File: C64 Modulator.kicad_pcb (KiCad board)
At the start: 2 copper layers, 63.5 x 63.4 mm, 36 parts, among them J1 Power, J10 , J11 , J12 , J13 , J14 , J2 8765, J3 4321, J4 AUD_STEREO, J5 TRS_3.5mm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

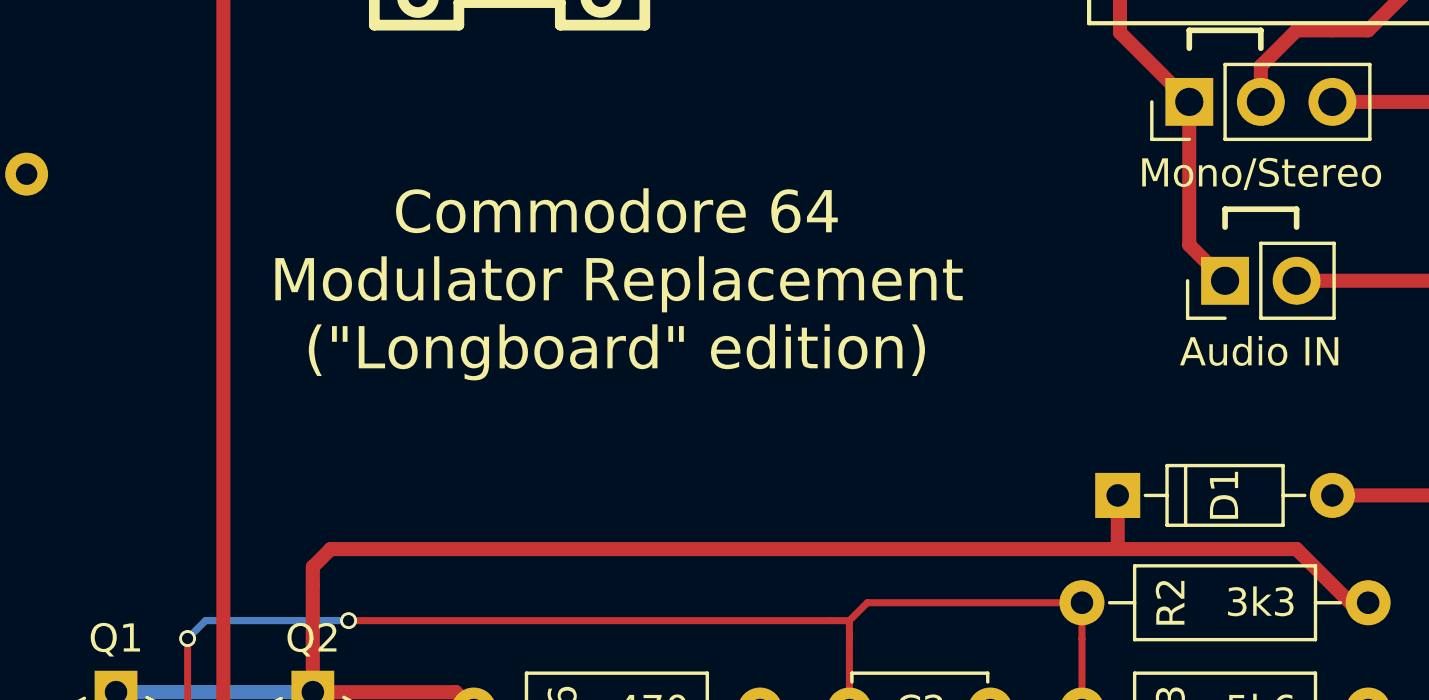
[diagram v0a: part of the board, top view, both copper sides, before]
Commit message: Added component notices to PCB
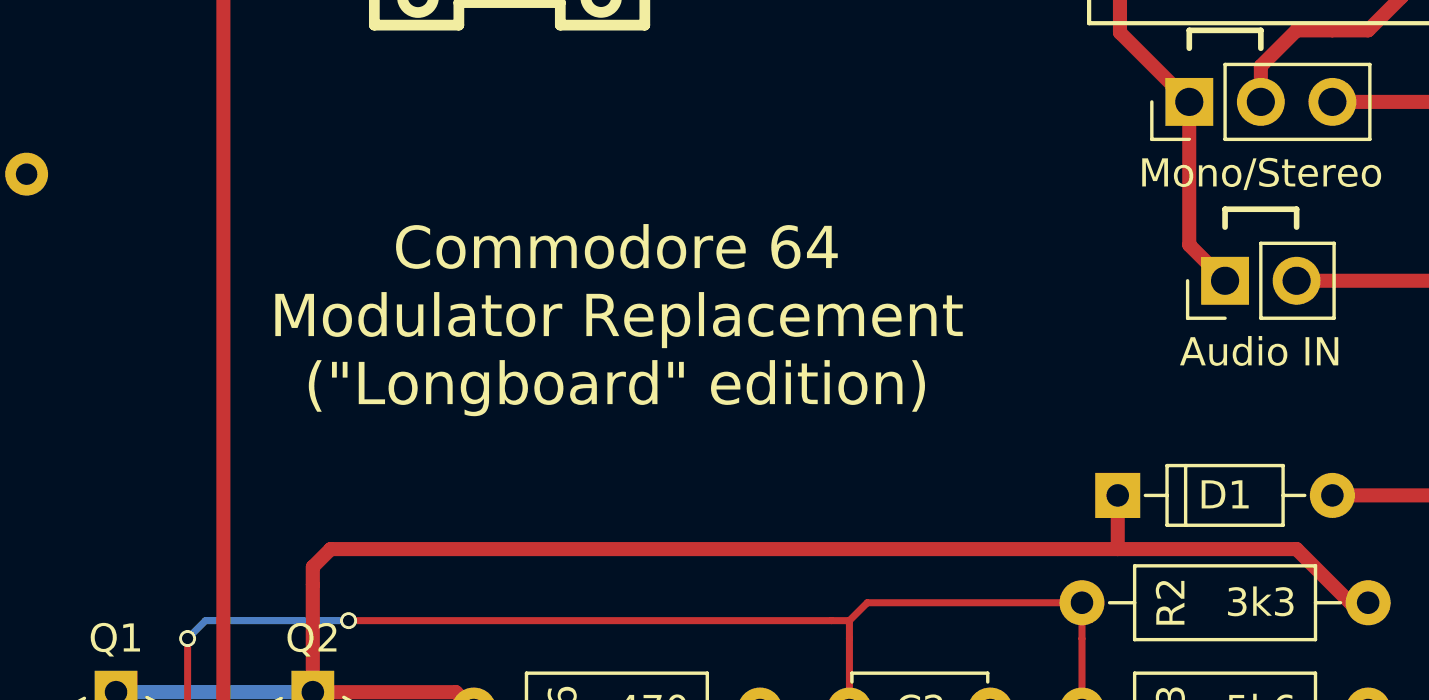
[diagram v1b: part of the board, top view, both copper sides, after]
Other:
- board text added: "L1 & D1 pads can be shorted, C2 & C3 can be left out."
- board text added: "L2, C6, R8, R11 & RCA can be left out if composite video is not required."
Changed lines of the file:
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@@
     (links 53)
     (no_connects 0)
-    (area 113.03 50.092 185.683334 130.175001)
+    (area 118.669999 62.154999 182.360001 125.745001)
     (thickness 1.6)
-    (drawings 54)
+    (drawings 125)
     (tracks 114)
     (zones 0)
@@
       (effects (font (size 1 1) (thickness 0.15)))
     )
-    (fp_text value 68pF (at 2.54 -1.27 180) (layer B.SilkS)
+    (fp_text value 68pF (at 2.54 -1.905 180) (layer B.SilkS)
       (effects (font (size 1 1) (thickness 0.15)) (justify mirror))
     )
@@
     (descr "D, DO-35_SOD27 series, Axial, Horizontal, pin pitch=7.62mm, , length*diameter=4*2mm^2, , http://www.diodes.com/_files/packages/DO-35.pdf")
     (tags "D DO-35_SOD27 series Axial Horizontal pin pitch 7.62mm  length 4mm diameter 2mm")
-    (fp_text reference D1 (at 3.81 0 90) (layer F.SilkS)
-      (effects (font (size 1 1) (thickness 0.15)))
-    )
-    (fp_text value 1n4148 (at 3.81 0) (layer B.SilkS)
+    (fp_text reference D1 (at 3.81 0) (layer F.SilkS)
+      (effects (font (size 1 1) (thickness 0.15)))
+    )
+    (fp_text value 1n4148 (at 3.81 1.27) (layer B.SilkS)
       (effects (font (size 1 1) (thickness 0.15)) (justify mirror))
     )
-    (fp_text user %R (at 3.81 0 90) (layer F.Fab)
+    (fp_text user %R (at 3.81 0 180) (layer F.Fab)
       (effects (font (size 1 1) (thickness 0.15)))
     )
@@
       (effects (font (size 1 1) (thickness 0.15)))
     )
-    (fp_text value 1n4148 (at 3.81 0 180) (layer B.SilkS)
+    (fp_text value 1n4148 (at 3.81 -1.27 180) (layer B.SilkS)
       (effects (font (size 1 1) (thickness 0.15)) (justify mirror))
     )
@@
     )
   )
+  (gr_line (start 165.735 102.235) (end 165.1 102.235) (angle 90) (layer B.SilkS) (width 0.2))
+  (gr_line (start 165.1 101.6) (end 165.735 101.6) (angle 90) (layer B.SilkS) (width 0.2))
+  (gr_line (start 161.925 102.235) (end 161.29 102.235) (angle 90) (layer B.SilkS) (width 0.2))
+  (gr_line (start 161.29 101.6) (end 161.925 101.6) (angle 90) (layer B.SilkS) (width 0.2))
+  (gr_line (start 163.83 102.235) (end 164.465 102.235) (angle 90) (layer B.SilkS) (width 0.2))
+  (gr_line (start 163.83 101.6) (end 164.465 101.6) (angle 90) (layer B.SilkS) (width 0.2))
+  (gr_line (start 164.465 90.17) (end 165.1 90.17) (angle 90) (layer B.SilkS) (width 0.2))
+  (gr_line (start 163.195 90.17) (end 163.83 90.17) (angle 90) (layer B.SilkS) (width 0.2))
+  (gr_line (start 161.925 90.17) (end 162.56 90.17) (angle 90) (layer B.SilkS) (width 0.2))
+  (gr_line (start 162.56 101.6) (end 163.195 101.6) (angle 90) (layer B.SilkS) (width 0.2))
+  (gr_line (start 153.67 86.995) (end 153.67 87.63) (angle 90) (layer B.SilkS) (width 0.2))
+  (gr_line (start 153.67 85.725) (end 153.67 86.36) (angle 90) (layer B.SilkS) (width 0.2))
+  (gr_line (start 153.035 86.995) (end 153.035 87.63) (angle 90) (layer B.SilkS) (width 0.2))
+  (gr_line (start 153.035 85.725) (end 153.035 86.36) (angle 90) (layer B.SilkS) (width 0.2))
+  (gr_line (start 164.465 90.805) (end 165.1 90.805) (angle 90) (layer B.SilkS) (width 0.2))
+  (gr_line (start 163.195 90.805) (end 163.83 90.805) (angle 90) (layer B.SilkS) (width 0.2))
+  (gr_line (start 161.925 90.805) (end 162.56 90.805) (angle 90) (layer B.SilkS) (width 0.2))
+  (gr_line (start 160.655 90.17) (end 161.29 90.805) (angle 90) (layer B.SilkS) (width 0.2))
+  (gr_line (start 160.655 90.805) (end 161.29 90.17) (angle 90) (layer B.SilkS) (width 0.2))
+  (gr_line (start 159.385 101.6) (end 160.02 102.235) (angle 90) (layer B.SilkS) (width 0.2))
+  (gr_line (start 159.385 102.235) (end 160.02 101.6) (angle 90) (layer B.SilkS) (width 0.2))
+  (gr_line (start 153.67 83.185) (end 153.035 83.82) (angle 90) (layer B.SilkS) (width 0.2))
+  (gr_line (start 153.035 83.185) (end 153.67 83.82) (angle 90) (layer B.SilkS) (width 0.2))
+  (gr_line (start 153.035 76.835) (end 153.67 77.47) (angle 90) (layer B.SilkS) (width 0.2))
+  (gr_line (start 153.67 76.835) (end 153.035 76.835) (angle 90) (layer B.SilkS) (width 0.2))
+  (gr_line (start 153.035 77.47) (end 153.67 76.835) (angle 90) (layer B.SilkS) (width 0.2))
+  (gr_line (start 153.67 76.835) (end 153.035 76.835) (angle 90) (layer B.SilkS) (width 0.2))
+  (gr_line (start 153.67 77.47) (end 153.67 76.835) (angle 90) (layer B.SilkS) (width 0.2))
+  (gr_line (start 153.035 77.47) (end 153.67 77.47) (angle 90) (layer B.SilkS) (width 0.2))
+  (gr_line (start 153.035 76.835) (end 153.035 77.47) (angle 90) (layer B.SilkS) (width 0.2))
+  (gr_line (start 137.795 101.6) (end 138.43 102.235) (angle 90) (layer B.SilkS) (width 0.2))
+  (gr_line (start 138.43 101.6) (end 137.795 102.235) (angle 90) (layer B.SilkS) (width 0.2))
+  (gr_line (start 137.795 105.41) (end 138.43 106.045) (angle 90) (layer B.SilkS) (width 0.2))
+  (gr_line (start 137.795 106.045) (end 138.43 105.41) (angle 90) (layer B.SilkS) (width 0.2))
+  (gr_line (start 129.54 109.22) (end 130.175 109.855) (angle 90) (layer B.SilkS) (width 0.2))
+  (gr_line (start 129.54 109.855) (end 130.175 109.22) (angle 90) (layer B.SilkS) (width 0.2))
+  (gr_line (start 137.795 109.22) (end 138.43 109.855) (angle 90) (layer B.SilkS) (width 0.2))
+  (gr_line (start 137.795 109.855) (end 138.43 109.22) (angle 90) (layer B.SilkS) (width 0.2))
+  (gr_line (start 138.43 109.855) (end 137.795 109.855) (angle 90) (layer B.SilkS) (width 0.2))
+  (gr_line (start 138.43 109.22) (end 138.43 109.855) (angle 90) (layer B.SilkS) (width 0.2))
+  (gr_line (start 137.795 109.22) (end 138.43 109.22) (angle 90) (layer B.SilkS) (width 0.2))
+  (gr_line (start 137.795 109.855) (end 137.795 109.22) (angle 90) (layer B.SilkS) (width 0.2))
+  (gr_line (start 138.43 106.045) (end 137.795 106.045) (angle 90) (layer B.SilkS) (width 0.2))
+  (gr_line (start 138.43 105.41) (end 138.43 106.045) (angle 90) (layer B.SilkS) (width 0.2))
+  (gr_line (start 137.795 105.41) (end 138.43 105.41) (angle 90) (layer B.SilkS) (width 0.2))
+  (gr_line (start 137.795 106.045) (end 137.795 105.41) (angle 90) (layer B.SilkS) (width 0.2))
+  (gr_line (start 130.175 109.855) (end 129.54 109.855) (angle 90) (layer B.SilkS) (width 0.2))
+  (gr_line (start 130.175 109.22) (end 130.175 109.855) (angle 90) (layer B.SilkS) (width 0.2))
+  (gr_line (start 129.54 109.22) (end 130.175 109.22) (angle 90) (layer B.SilkS) (width 0.2))
+  (gr_line (start 129.54 109.855) (end 129.54 109.22) (angle 90) (layer B.SilkS) (width 0.2))
+  (gr_line (start 138.43 102.235) (end 137.795 102.235) (angle 90) (layer B.SilkS) (width 0.2))
+  (gr_line (start 138.43 101.6) (end 138.43 102.235) (angle 90) (layer B.SilkS) (width 0.2))
+  (gr_line (start 137.795 101.6) (end 138.43 101.6) (angle 90) (layer B.SilkS) (width 0.2))
+  (gr_line (start 137.795 102.235) (end 137.795 101.6) (angle 90) (layer B.SilkS) (width 0.2))
+  (gr_line (start 150.495 105.41) (end 151.13 106.045) (angle 90) (layer B.SilkS) (width 0.2))
+  (gr_line (start 151.13 105.41) (end 150.495 106.045) (angle 90) (layer B.SilkS) (width 0.2))
+  (gr_line (start 151.13 97.79) (end 150.495 98.425) (angle 90) (layer B.SilkS) (width 0.2))
+  (gr_line (start 150.495 97.79) (end 151.13 98.425) (angle 90) (layer B.SilkS) (width 0.2))
+  (gr_line (start 163.195 102.235) (end 162.56 102.235) (angle 90) (layer B.SilkS) (width 0.2))
+  (gr_line (start 121.92 88.265) (end 121.92 83.185) (angle 90) (layer B.SilkS) (width 0.2))
+  (gr_line (start 152.4 88.265) (end 121.92 88.265) (angle 90) (layer B.SilkS) (width 0.2))
+  (gr_line (start 152.4 83.185) (end 152.4 88.265) (angle 90) (layer B.SilkS) (width 0.2))
+  (gr_line (start 121.92 83.185) (end 152.4 83.185) (angle 90) (layer B.SilkS) (width 0.2))
+  (gr_line (start 152.4 81.915) (end 121.92 81.915) (angle 90) (layer B.SilkS) (width 0.2))
+  (gr_line (start 152.4 76.835) (end 121.92 76.835) (angle 90) (layer B.SilkS) (width 0.2))
+  (gr_line (start 152.4 76.835) (end 152.4 81.915) (angle 90) (layer B.SilkS) (width 0.2))
+  (gr_line (start 121.92 77.47) (end 121.92 76.835) (angle 90) (layer B.SilkS) (width 0.2))
+  (gr_line (start 121.92 81.915) (end 121.92 77.47) (angle 90) (layer B.SilkS) (width 0.2))
+  (gr_line (start 121.92 77.47) (end 121.92 81.915) (angle 90) (layer B.SilkS) (width 0.2))
+  (gr_text "L1 & D1 pads can be shorted,\nC2 & C3 can be left out." (at 137.16 85.725) (layer B.SilkS)
+    (effects (font (size 1 1) (thickness 0.15)) (justify mirror))
+  )
+  (gr_text "L2, C6, R8, R11 & RCA can be left\nout if composite video is not required." (at 137.16 79.375) (layer B.SilkS)
+    (effects (font (size 1 1) (thickness 0.15)) (justify mirror))
+  )
   (gr_text GND (at 178.435 123.825) (layer F.SilkS)
     (effects (font (size 0.8 0.8) (thickness 0.15)))
@@
     (effects (font (size 0.8 0.8) (thickness 0.15)))
   )
-  (gr_text "Commodore 64\nModulator Replacement\n(\"Longboard\" edition)" (at 140.97 83.185) (layer F.SilkS)
+  (gr_text "Commodore 64\nModulator Replacement\n(\"Longboard\" edition)" (at 140.97 84.455) (layer F.SilkS)
     (effects (font (size 1.5 1.5) (thickness 0.15)))
   )

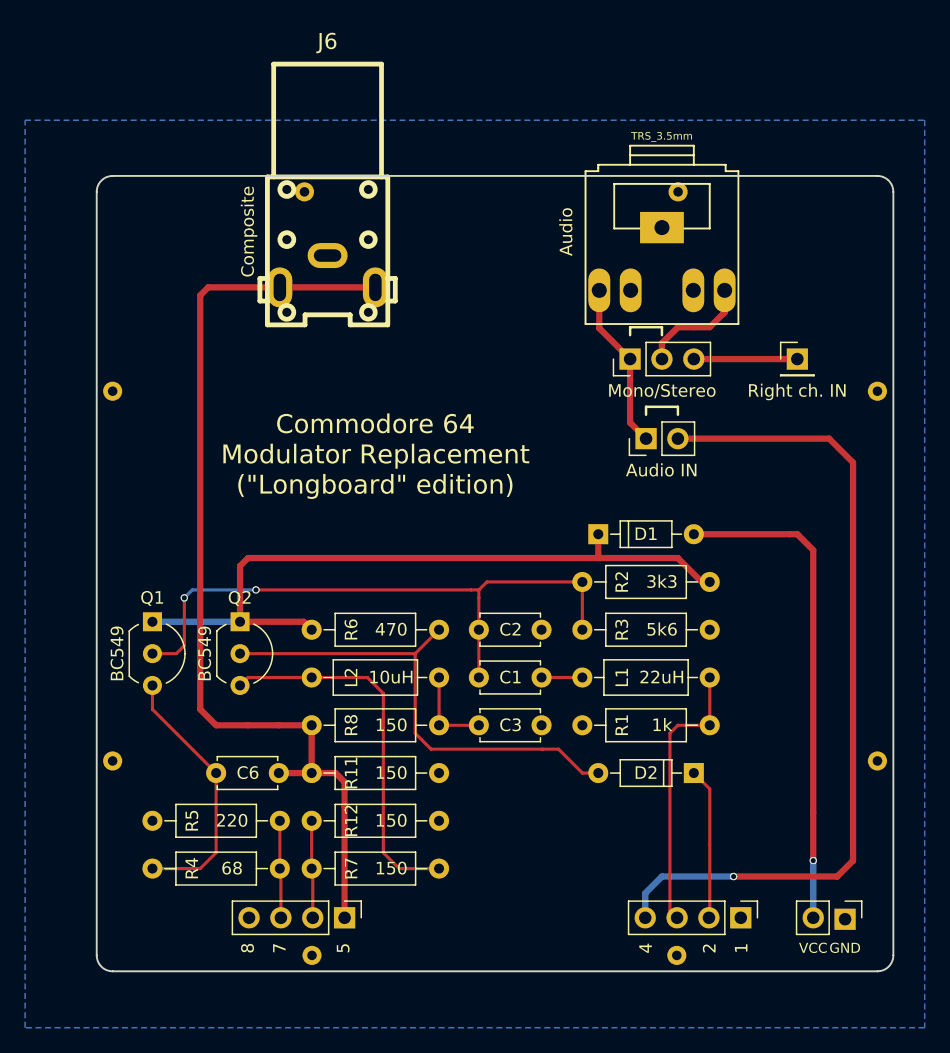
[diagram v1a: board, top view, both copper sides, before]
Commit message: Added 5v regulator to board
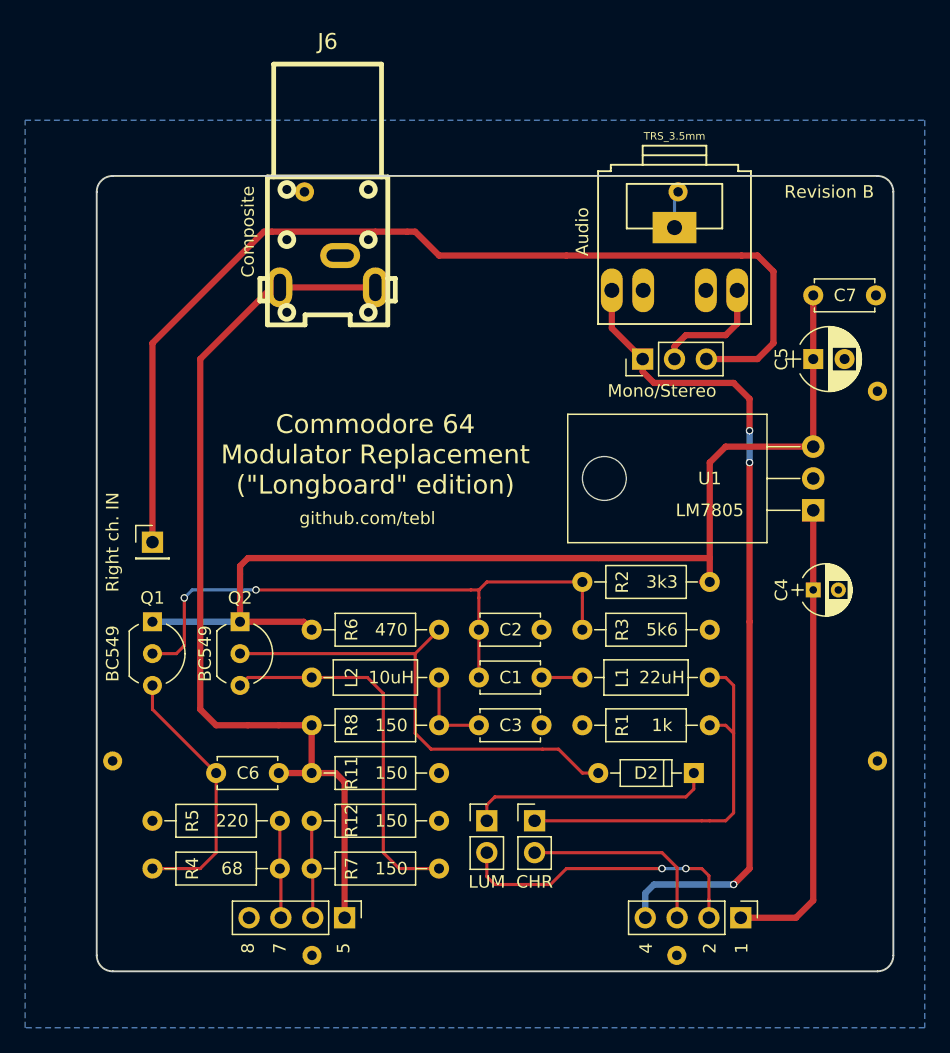
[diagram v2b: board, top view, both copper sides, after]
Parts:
- removed D1: 1n4148, Diodes_THT:D_DO-35_SOD27_P7.62mm_Horizontal
- removed J1: Power, Pin_Headers:Pin_Header_Straight_1x02_Pitch2.54mm
- removed J7: , anchors:anchor_circle
- removed JP1: AUD_SEL, Pin_Headers:Pin_Header_Straight_1x02_Pitch2.54mm
- added C4: 10uF, Capacitors_THT:CP_Radial_D4.0mm_P2.00mm, F.Cu at (175.9, 95.2)
- added C5: 100uF, Capacitors_THT:CP_Radial_D5.0mm_P2.50mm, F.Cu at (175.9, 76.8)
- added C7: 100nF, Capacitors_THT:C_Disc_D4.7mm_W2.5mm_P5.00mm, F.Cu at (175.9, 71.8)
- added JP3: CHR, Pin_Headers:Pin_Header_Straight_1x02_Pitch2.54mm, F.Cu at (153.7, 113.7)
- added JP4: LUM, Pin_Headers:Pin_Header_Straight_1x02_Pitch2.54mm, F.Cu at (149.9, 113.7)
- added U1: LM7805, TO_SOT_Packages_THT:TO-220-3_Horizontal, F.Cu at (175.9, 88.9)
- moved J4 53.5 mm to (123.2, 91.4)
- moved J5 1.00 mm to (164.8, 67.9)
- moved JP2 1.00 mm to (162.3, 76.8)
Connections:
- J3 pad 1: (no net) -> +9V
- J3 pad 2: LUMA_IN -> Net-(J3-Pad2)
- J3 pad 3: CHROMA_IN -> Net-(J3-Pad3)
- J5 pad 5: /AUD_L -> AUDIO_IN
- JP2 pad 1: /AUD_L -> AUDIO_IN
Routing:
- net Net-(J4-Pad1): track 8.25 -> 82.0 mm
- net Net-(D1-Pad2): track 39.4 -> 0.00 mm, vias 1 -> 0
- net +9V: track 0.00 -> 37.5 mm
- net VCC: track 57.8 -> 86.1 mm
- net Net-(J3-Pad2): track 0.00 -> 24.1 mm, vias 0 -> 2
- net Net-(J3-Pad3): track 0.00 -> 15.9 mm
- net /AUD_L: track 13.4 -> 0.00 mm
- net CHROMA_IN: track 22.3 -> 30.6 mm
- net LUMA_IN: track 12.1 -> 19.6 mm
- net COMPOSITE: track 76.8 -> 73.9 mm
- net GND: track 0.00 -> 2.97 mm
- net AUDIO_IN: track 66.1 -> 65.5 mm, vias 1 -> 3
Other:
- board text added: "9v Un."
- board text added: "Revision B"
- board text added: "github.com/tebl"
- board text removed: "Unused"
- board text removed: "VCC"
